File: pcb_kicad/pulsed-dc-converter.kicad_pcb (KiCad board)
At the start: 2 copper layers, 72 x 50 mm, 31 parts, among them J1 Conn_01x02_Female, J2 AttinyPins2, J3 AttinyPins1, J4 Conn_01x02_Female, M1 Motor_DC, Q1 IRLZ34N or RFP14N05, U1 ATtiny25-20PU, U2 LP2950-5.0

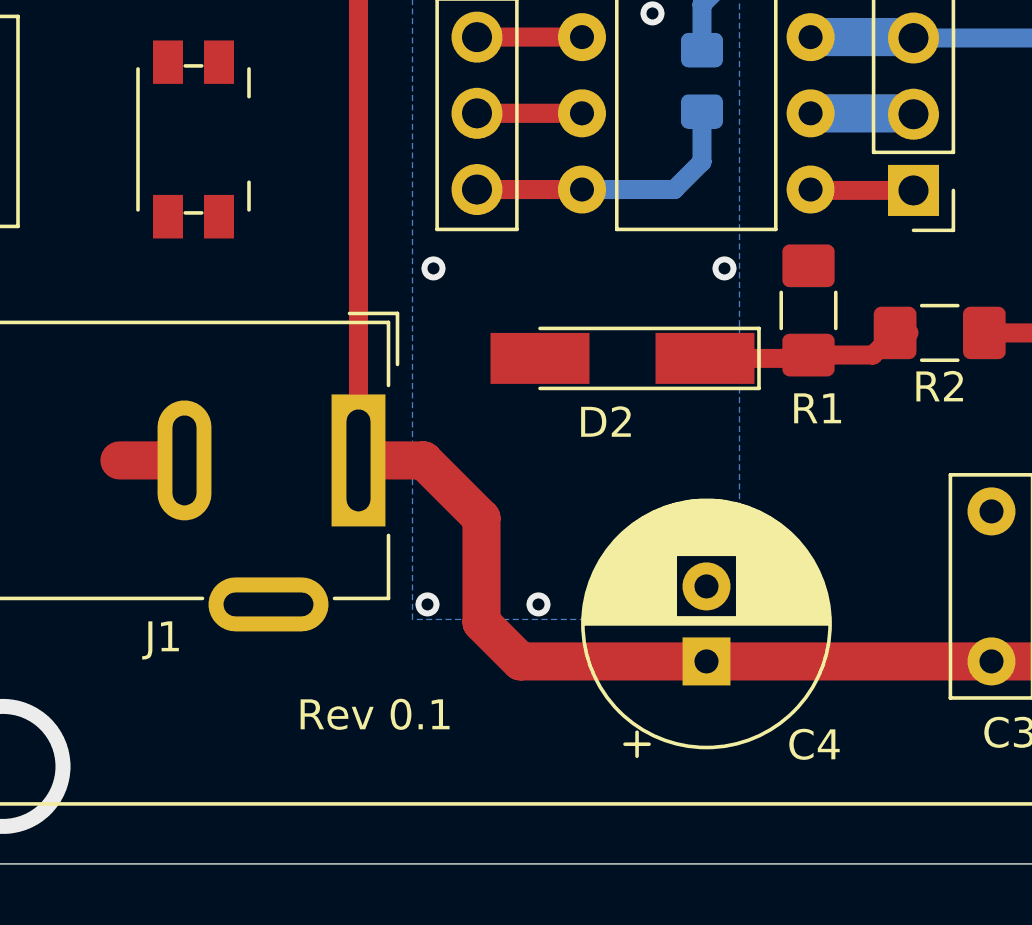
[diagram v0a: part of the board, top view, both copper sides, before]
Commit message: Final TESTED, working PCB - Tested with following population alternatives and current git attiny code:
C4: 360u + 100u on TP0 reserve slot (no fitting form factor 470u Capacitor with >20V tolerance was available)
D3: Wire
R2: 22 (33 was not available, but should work either way)
R6: 100k
R7: 10.5k
R4: 22.1k
R5: 10k

PCB was manufactured at JLCPCB using their recommended settings to create Gerber file with KiCad 5:
 -> https://support.jlcpcb.com/article/149-how-to-generate-gerber-and-drill-files-in-kicad
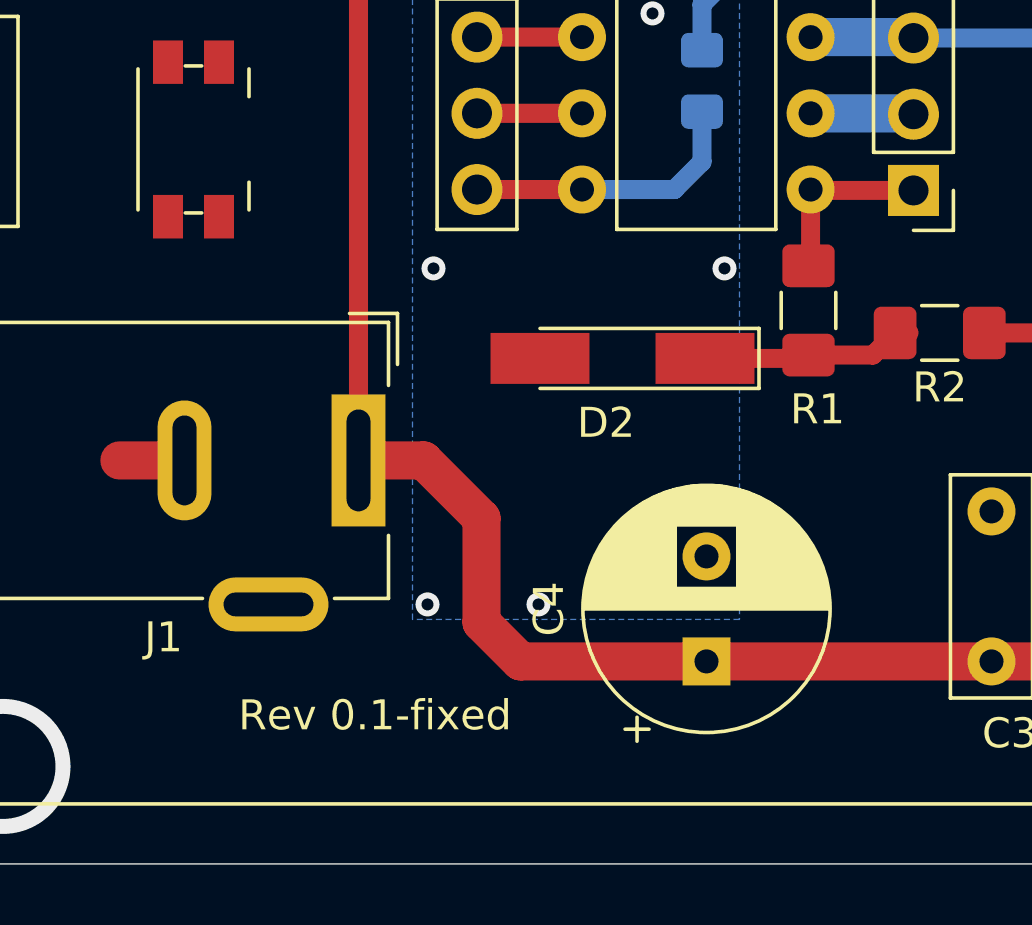
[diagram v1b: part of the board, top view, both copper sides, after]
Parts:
- C4: footprint Capacitor_THT:CP_Radial_D8.0mm_P2.50mm -> Capacitor_THT:CP_Radial_D8.0mm_P3.50mm
- D3: value 5.6V -> 5.6V or Wire
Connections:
- Q1 pad : Net-(D1-Pad2) -> (no net)
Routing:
- net Net-(J2-Pad1): track 3.68 -> 6.25 mm
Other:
- board text added: "Rev 0.1-fixed"
- board text removed: "Rev 0.1"

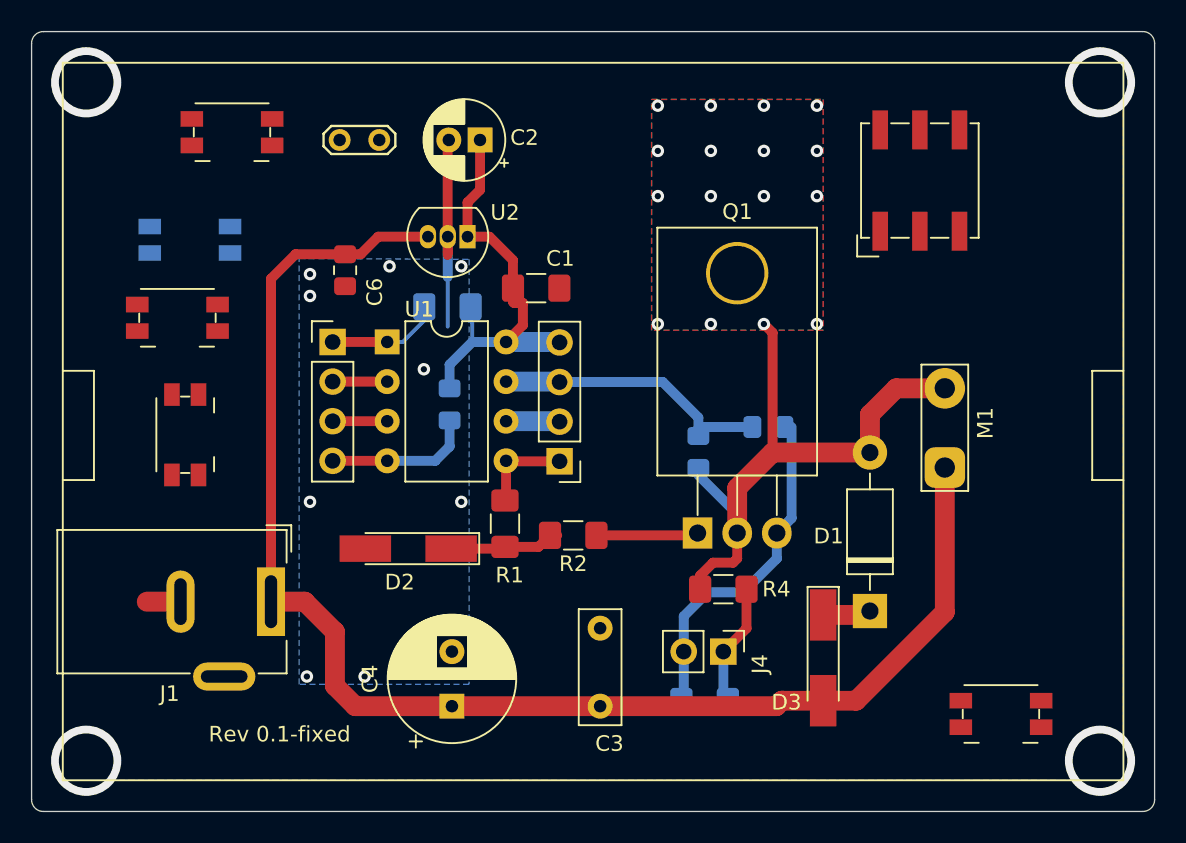
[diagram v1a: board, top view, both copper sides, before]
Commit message: Various PCB adjustments for a better Rev 02
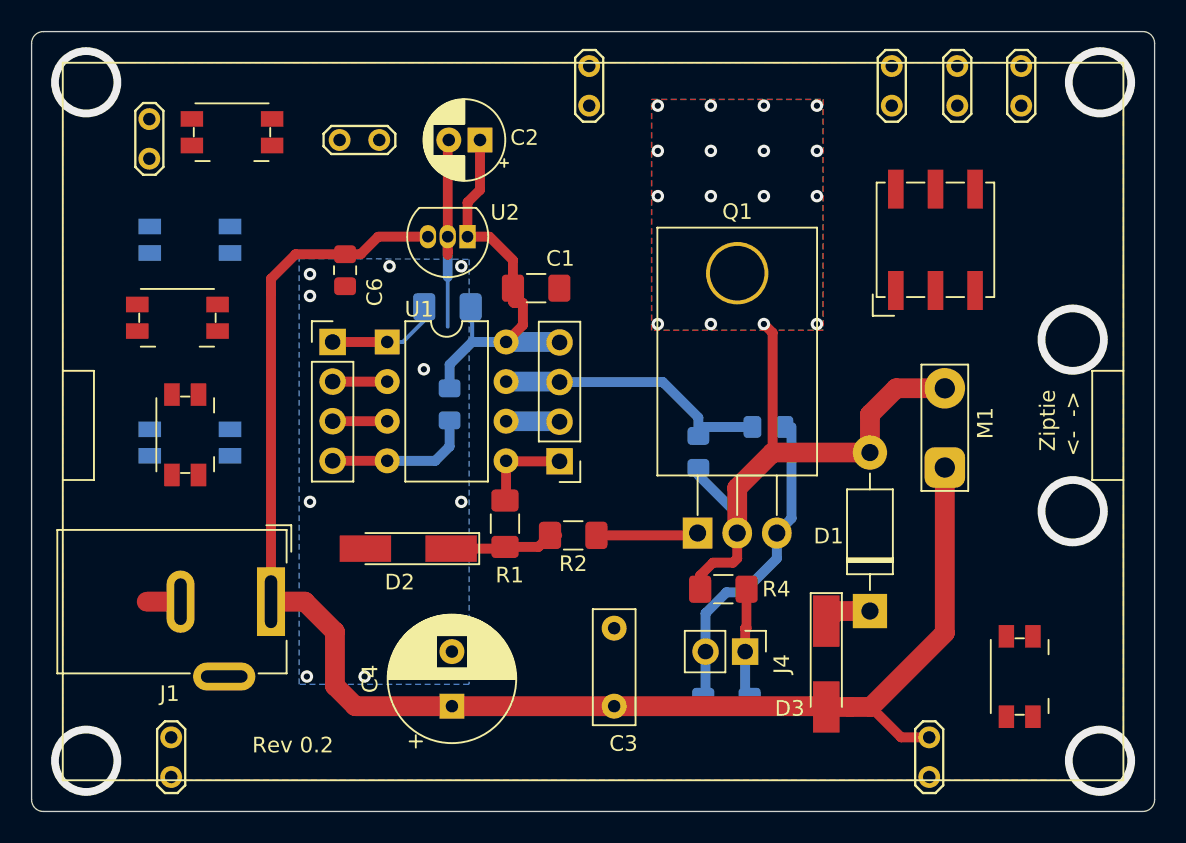
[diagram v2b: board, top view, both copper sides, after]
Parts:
- removed the Reserved at (172.4, 124.0)
- added REF**: TP0, TestPoint:TestPoint_2Pads_Pitch2.54mm_Drill0.8mm, F.Cu at (167.8, 125.5)
- added REF**: TP0, TestPoint:TestPoint_2Pads_Pitch2.54mm_Drill0.8mm, F.Cu at (119.2, 125.5)
- added REF**: TP0, TestPoint:TestPoint_2Pads_Pitch2.54mm_Drill0.8mm, F.Cu at (165.4, 85.0)
- added REF**: TP0, TestPoint:TestPoint_2Pads_Pitch2.54mm_Drill0.8mm, F.Cu at (169.6, 85.0)
- added REF**: TP0, TestPoint:TestPoint_2Pads_Pitch2.54mm_Drill0.8mm, F.Cu at (173.7, 85.0)
- added REF**: TP0, TestPoint:TestPoint_2Pads_Pitch2.54mm_Drill0.8mm, F.Cu at (146.0, 85.0)
- added REF**: TP0, TestPoint:TestPoint_2Pads_Pitch2.54mm_Drill0.8mm, F.Cu at (117.8, 88.4)
- added Reserved: Panasonic_EVQPUK_EVQPUB, Button_Switch_SMD:Panasonic_EVQPUK_EVQPUB, B.Cu at (120.4, 106.6)
- added Reserved: Panasonic_EVQPUK_EVQPUB, Button_Switch_SMD:Panasonic_EVQPUK_EVQPUB, F.Cu at (173.6, 121.6)
- moved Reserved 3.93 mm to (168.2, 93.6)
- moved J4 1.40 mm to (156.0, 120.0)
- moved R5 1.40 mm to (154.8, 123.2)
- moved C3 0.90 mm to (147.6, 123.5)
- moved D3 0.45 mm to (161.2, 120.8)
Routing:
- net +12V: track 91.7 -> 97.0 mm
- net 0: track 46.8 -> 45.6 mm, vias 13 -> 15
- net Net-(J4-Pad1): track 7.53 -> 7.00 mm
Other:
- board text added: "Rev 0.2"
- board text added: "Ziptie <- ->"
- board text removed: "Rev 0.1-fixed"
